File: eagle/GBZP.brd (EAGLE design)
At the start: 70 x 57.5 mm, 45 parts, among them CN1 USB-SMD-NS, J3 battery, X3 16MHz

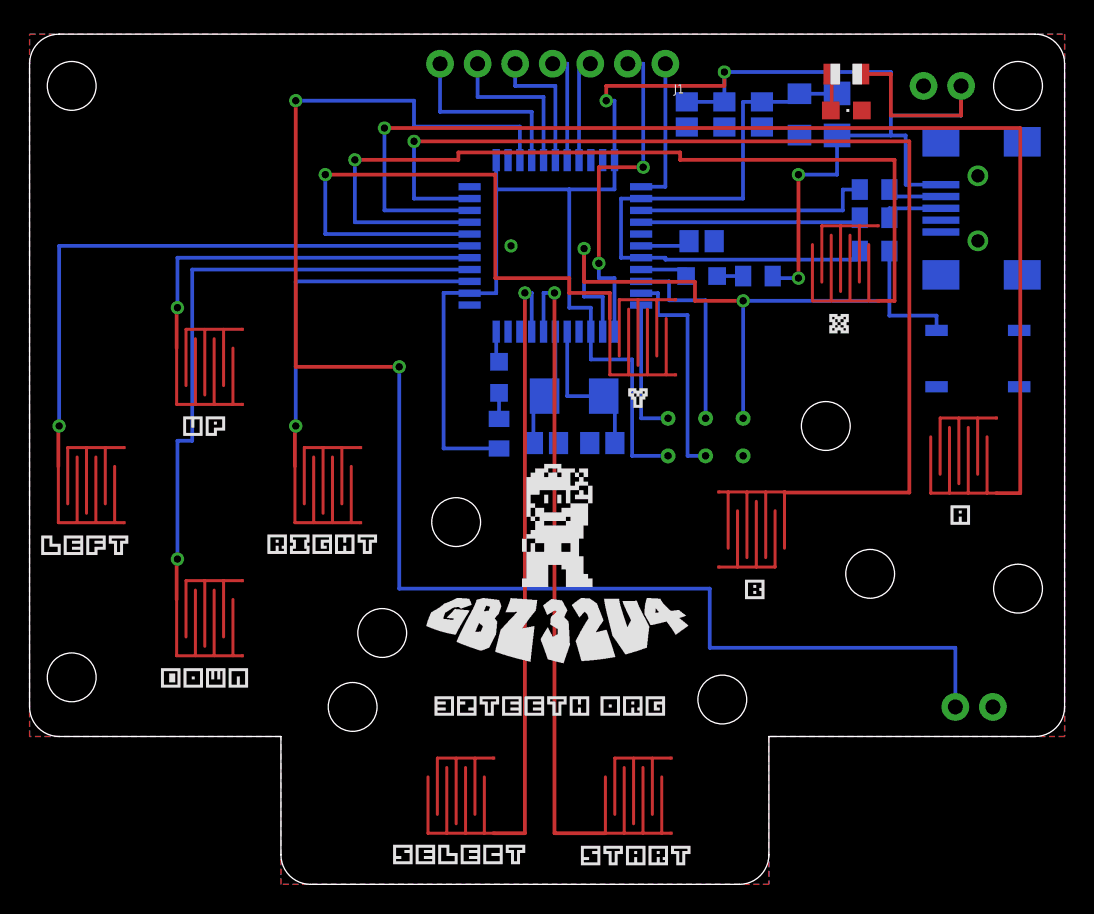
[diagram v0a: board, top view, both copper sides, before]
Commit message: new pinout to match GBZ project
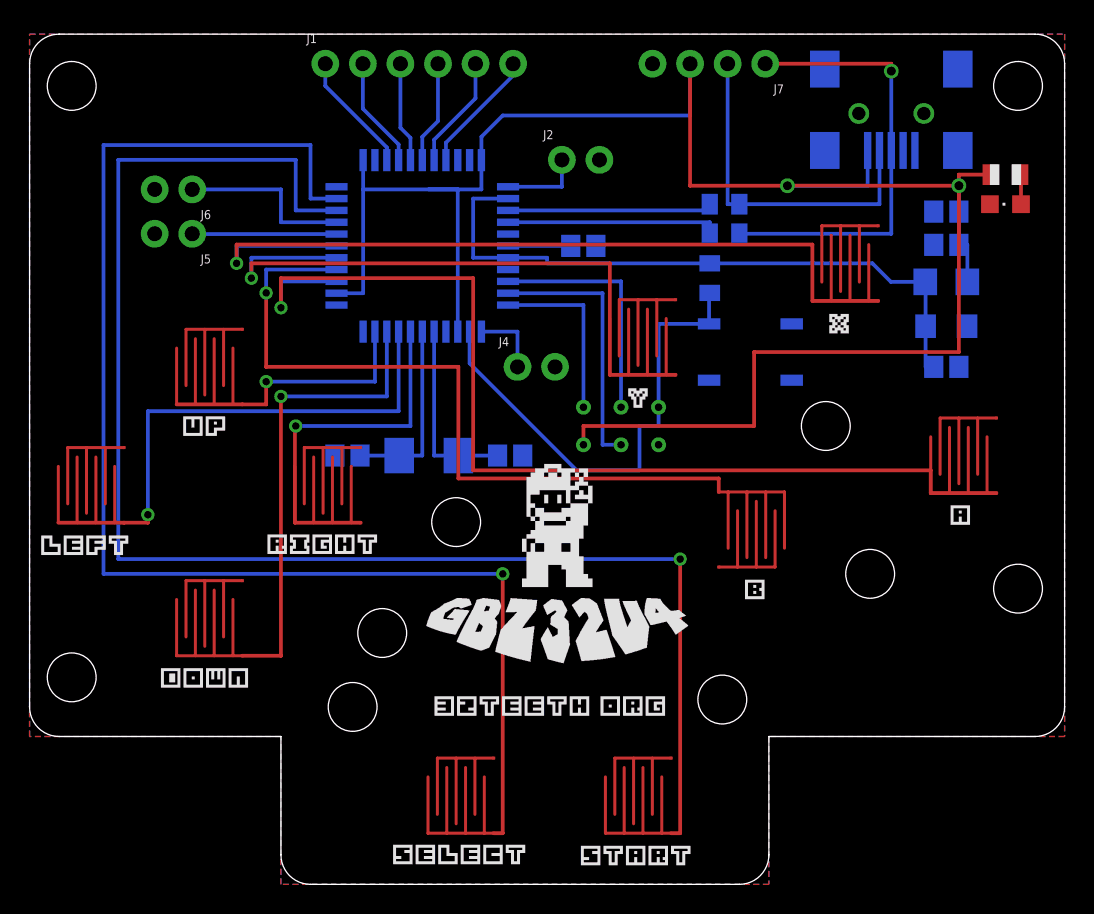
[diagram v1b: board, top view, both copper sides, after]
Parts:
- removed J3: battery, SparkFun-Connectors:1X02_NO_SILK
- removed JP2: Speaker, SparkFun-Connectors:1X02_NO_SILK
- removed LEDRX, LEDTX: LED, adafruit:CHIPLED_0805
- removed R4, R5: 100ohm, adafruit:R0805
- added J2, J4, J5, J6: (no value), SparkFun-Connectors:1X02_NO_SILK
- added J7: (no value), SparkFun-Connectors:1X04_NO_SILK
- J1: device SparkFun-Connectors:1X07_NO_SILK -> SparkFun-Connectors:1X06_NO_SILK
- moved J1 23.0 mm to (20.0, 55.5), turned to 0 degrees
- moved C4 21.1 mm to (62.0, 35.0), turned to 180 degrees
- moved C7 18.7 mm to (62.0, 45.5), turned to 0 degrees
- moved C5 17.4 mm to (62.0, 37.8), turned to 0 degrees
- moved C6 17.4 mm to (62.0, 43.2), turned to 0 degrees
- moved S1 15.4 mm to (48.8, 36.0)
- moved L1 13.5 mm to (62.0, 40.8), turned to 0 degrees
- moved C2 13.5 mm to (21.5, 29.0), turned to 0 degrees
- moved R2 12.7 mm to (66.0, 48.0), turned to 180 degrees
- moved LEDPWR 12.5 mm to (66.0, 46.0), turned to 90 degrees
- moved R6 11.3 mm to (46.0, 41.0), turned to 270 degrees
- moved X3 10.6 mm to (27.0, 29.0)
- moved R3 10.2 mm to (47.0, 44.0)
- moved R1 10.2 mm to (47.0, 46.0)
- moved U$2 9.00 mm to (26.6, 43.2)
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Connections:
- removed net A0/SPEAKER: JP2.2, U$2.36
- removed net D0/RX: U$2.20
- removed net D1/TX: U$2.21
- removed net D10/X: BTN-X.2, U$2.30
- removed net D11: J1.2, U$2.12
- removed net D12/DOWN: DIR-D.2, U$2.26
- removed net D13/B: BTN-B.2, U$2.32
- removed net D2/SELECT: BTN-SELECT.2, U$2.19
- removed net D3/START: BTN-START.2, U$2.18
- removed net D4/RIGHT: DIR-R.2, U$2.25
- removed net D5/A: BTN-A.2, U$2.31
- removed net D6/UP: DIR-U.2, U$2.27
- removed net D7: J1.1, U$2.1
- removed net D8/LEFT: DIR-L.2, U$2.28
- removed net D9/Y: BTN-Y.2, U$2.29
- removed net N$3: CN1.D+, R3.1
- removed net N$5: CN1.D-, R1.1
- removed net N$6: LEDRX.A, R4.1
- removed net N$7: LEDTX.A, R5.1
- new net A0: J1.1, U$2.36
- new net BTN_A: BTN-A.2, U$2.25
- new net BTN_B: BTN-B.2, U$2.26
- new net BTN_DOWN: DIR-D.2, U$2.20
- new net BTN_L1: J2.1, U$2.1
- new net BTN_L2: J4.1, U$2.12
- new net BTN_LEFT: DIR-L.2, U$2.19
- new net BTN_R1: J5.1, U$2.29
- new net BTN_R2: J6.1, U$2.30
- new net BTN_RIGHT: DIR-R.2, U$2.18
- new net BTN_SELECT: BTN-SELECT.2, U$2.32
- new net BTN_START: BTN-START.2, U$2.31
- new net BTN_UP: DIR-U.2, U$2.21
- new net BTN_X: BTN-X.2, U$2.28
- new net BTN_Y: BTN-Y.2, U$2.27
- new net D+IN: CN1.D+, J7.1, R3.1
- new net D-IN: CN1.D-, J7.2, R1.1
- net A1: now also J1.2; no longer J1.7
- net A2: now also J1.3; no longer J1.6
- net A3: now also J1.4; no longer J1.5
- net A4: now also J1.5; no longer J1.4
- net A5: now also J1.6; no longer J1.3
- net GND: now also J2.2, J4.2, J5.2, J6.2, J7.4; no longer J3.2, JP2.1
- net RXLED: no longer LEDRX.C
- net TXLED: no longer LEDTX.C
- net VCC: now also J7.3; no longer J3.1, R4.2, R5.2
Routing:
- net A0/SPEAKER: track 104.8 -> 0.00 mm, vias 2 -> 0
- net BTN_START: track 0.00 -> 102.3 mm, vias 0 -> 1
- net BTN_SELECT: track 0.00 -> 93.5 mm, vias 0 -> 1
- net D5/A: track 80.6 -> 0.00 mm, vias 1 -> 0
- net D13/B: track 73.4 -> 0.00 mm, vias 1 -> 0
- net BTN_A: track 0.00 -> 70.5 mm, vias 0 -> 1
- net D10/X: track 60.1 -> 0.00 mm, vias 1 -> 0
- net BTN_X: track 0.00 -> 56.4 mm, vias 0 -> 1
- net BTN_B: track 0.00 -> 50.4 mm, vias 0 -> 1
- net BTN_Y: track 0.00 -> 44.4 mm, vias 0 -> 1
- net D3/START: track 43.3 -> 0.00 mm, vias 1 -> 0
- net D9/Y: track 42.8 -> 0.00 mm, vias 1 -> 0
- net D8/LEFT: track 42.7 -> 0.00 mm, vias 1 -> 0
- net D12/DOWN: track 42.1 -> 0.00 mm, vias 1 -> 0
- net D2/SELECT: track 41.7 -> 0.00 mm, vias 1 -> 0
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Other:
- board text added: "(WH) D+ (GR) D- (RD) VCC (BK) GND"
- board text added: "A5 A4 A3 A2 A1 A0"
- board text removed: "D7 D11 A5 A4 A3 A2 A1"

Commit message: Mon Apr  3 10:04:51 EDT 2017 - added new pin mapping
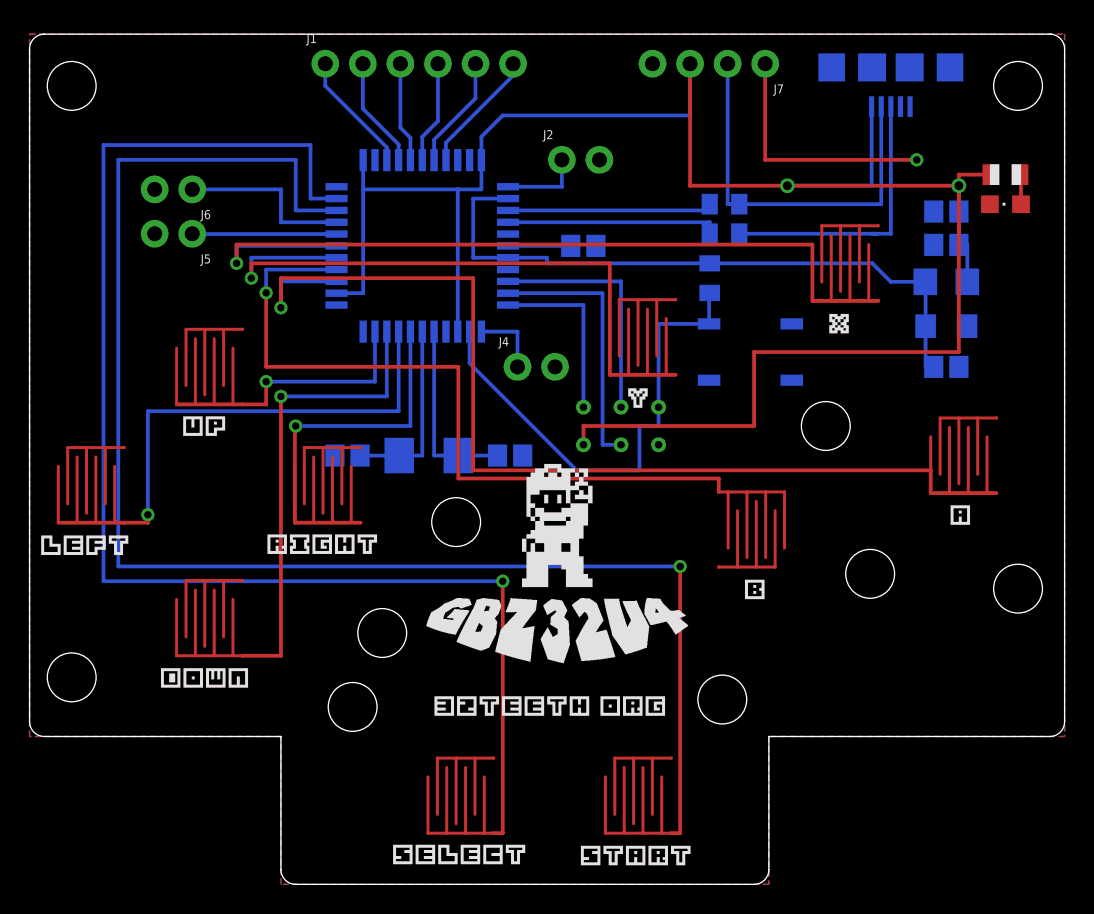
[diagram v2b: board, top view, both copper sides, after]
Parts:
- CN1: value USB-SMD-NS -> USB-MICROB; device SparkFun-Connectors:USB-MINIB-NOSTOP -> SparkFun-Connectors:USB-MICROB
- moved CN1 3.12 mm to (58.2, 55.2), turned to 180 degrees
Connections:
- net GND: now also CN1.MT1, CN1.MT2
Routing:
- net D+IN: track 30.3 -> 37.6 mm
- net D-IN: track 23.4 -> 26.5 mm
- net VCC: track 139.3 -> 140.5 mm
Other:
- outline, holes or cut-outs redrawn
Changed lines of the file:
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@@
 <board>
 <plain>
-<wire x1="70" y1="55.5" x2="70" y2="12" width="0" layer="20"/>
-<wire x1="70" y1="12" x2="68" y2="10" width="0" layer="20" curve="-90"/>
-<wire x1="68" y1="10" x2="50" y2="10" width="0" layer="20"/>
-<wire x1="70" y1="55.5" x2="68" y2="57.5" width="0" layer="20" curve="90"/>
-<wire x1="68" y1="57.5" x2="2" y2="57.5" width="0" layer="20"/>
-<wire x1="2" y1="57.5" x2="0" y2="55.5" width="0" layer="20" curve="90"/>
-<wire x1="0" y1="55.5" x2="0" y2="12" width="0" layer="20"/>
-<wire x1="0" y1="12" x2="2" y2="10" width="0" layer="20" curve="90"/>
-<wire x1="2" y1="10" x2="17" y2="10" width="0" layer="20"/>
-<wire x1="50" y1="10" x2="50" y2="2" width="0" layer="20"/>
-<wire x1="50" y1="2" x2="48" y2="0" width="0" layer="20" curve="-90"/>
-<wire x1="48" y1="0" x2="19" y2="0" width="0" layer="20"/>
-<wire x1="19" y1="0" x2="17" y2="2" width="0" layer="20" curve="-90"/>
-<wire x1="17" y1="2" x2="17" y2="10" width="0" layer="20"/>
+<wire x1="70" y1="11" x2="70" y2="56.5" width="0" layer="20"/>
+<wire x1="70" y1="56.5" x2="69" y2="57.5" width="0" layer="20" curve="90"/>
+<wire x1="69" y1="57.5" x2="1" y2="57.5" width="0" layer="20"/>
+<wire x1="70" y1="11" x2="69" y2="10" width="0" layer="20" curve="-90"/>
+<wire x1="69" y1="10" x2="50" y2="10" width="0" layer="20"/>
+<wire x1="1" y1="57.5" x2="0" y2="56.5" width="0" layer="20" curve="90"/>
+<wire x1="0" y1="56.5" x2="0" y2="11" width="0" layer="20"/>
+<wire x1="0" y1="11" x2="1" y2="10" width="0" layer="20" curve="90"/>
+<wire x1="1" y1="10" x2="17" y2="10" width="0" layer="20"/>
+<wire x1="50" y1="10" x2="50" y2="1" width="0" layer="20"/>
+<wire x1="50" y1="1" x2="49" y2="0" width="0" layer="20" curve="-90"/>
+<wire x1="49" y1="0" x2="18" y2="0" width="0" layer="20"/>
+<wire x1="18" y1="0" x2="17" y2="1" width="0" layer="20" curve="-90"/>
+<wire x1="17" y1="1" x2="17" y2="10" width="0" layer="20"/>
 <rectangle x1="27.3846" y1="11.4002" x2="28.7054" y2="11.451" layer="21"/>
 <rectangle x1="28.9086" y1="11.4002" x2="30.2294" y2="11.451" layer="21"/>
@@
 <element name="C6" library="adafruit" package="C0805" value="0.1uF" x="62" y="43.25" smashed="yes" rot="MR0"/>
 <element name="C7" library="adafruit" package="C0805" value="0.1uF" x="62" y="45.5" smashed="yes" rot="MR0"/>
-<element name="CN1" library="SparkFun-Connectors" package="USB-MINIB-NOSTOP" value="USB-SMD-NS" x="58.28" y="52.135" smashed="yes" rot="MR270"/>
+<element name="CN1" library="SparkFun-Connectors" package="USB-MICROB" value="USB-MICROB" x="58.25" y="55.25" smashed="yes" rot="MR180">
+<attribute name="PROD_ID" value="CONN-09505" x="58.25" y="55.25" size="1.778" layer="28" rot="MR180" display="off"/>
+</element>
 <element name="R2" library="adafruit" package="R0805" value="100ohm" x="66" y="48" smashed="yes" rot="R180"/>
 <element name="LEDPWR" library="adafruit" package="CHIPLED_0805" value="LED" x="66" y="46" smashed="yes" rot="R90"/>
@@
 <contactref element="J6" pad="2"/>
 <contactref element="J7" pad="4"/>
+<contactref element="CN1" pad="MT1"/>
+<contactref element="CN1" pad="MT2"/>
 <wire x1="38.3" y1="43.18" x2="39.88" y2="39.54" width="0" layer="19" extent="1-16"/>
 <wire x1="32.36" y1="43.98" x2="29.76" y2="48.98" width="0" layer="19" extent="16-16"/>
@@
 <wire x1="44.67" y1="47.25" x2="51.25" y2="47.25" width="0.254" layer="1"/>
 <wire x1="62.85" y1="47.25" x2="51.25" y2="47.25" width="0.254" layer="1"/>
-<wire x1="56.68" y1="49.635" x2="56.68" y2="47.25" width="0.254" layer="16"/>
-<wire x1="56.68" y1="47.25" x2="51.25" y2="47.25" width="0.254" layer="16"/>
 <via x="51.25" y="47.25" extent="1-16" drill="0.6"/>
 <wire x1="62.85" y1="47.25" x2="62.85" y2="45.5" width="0.254" layer="16"/>
@@
 <wire x1="30.56" y1="47" x2="30.56" y2="48.98" width="0.254" layer="16"/>
 <wire x1="22.56" y1="48.98" x2="22.56" y2="47" width="0.254" layer="16"/>
-<wire x1="27" y1="47" x2="30.56" y2="47" width="0.254" layer="16"/>
-<wire x1="27" y1="47" x2="22.56" y2="47" width="0.254" layer="16"/>
+<wire x1="28.96" y1="47" x2="30.56" y2="47" width="0.254" layer="16"/>
+<wire x1="28.96" y1="47" x2="22.56" y2="47" width="0.254" layer="16"/>
 <wire x1="22.56" y1="47" x2="22.56" y2="39.98" width="0.254" layer="16"/>
 <wire x1="22.56" y1="39.98" x2="20.76" y2="39.98" width="0.254" layer="16"/>
@@
 <wire x1="62.85" y1="36" x2="62.85" y2="47.25" width="0.254" layer="1"/>
 <wire x1="49" y1="36" x2="62.85" y2="36" width="0.254" layer="1"/>
-<wire x1="28.96" y1="47" x2="27" y2="47" width="0.254" layer="16"/>
 <wire x1="28.96" y1="37.38" x2="28.96" y2="47" width="0.254" layer="16"/>
+<wire x1="56.95" y1="52.6" x2="56.95" y2="47.25" width="0.254" layer="16"/>
+<wire x1="56.95" y1="47.25" x2="51.25" y2="47.25" width="0.254" layer="16"/>
 </signal>
 <signal name="BTN_UP">
@@
 <contactref element="R3" pad="1"/>
 <contactref element="J7" pad="1"/>
-<wire x1="49.75" y1="55.5" x2="58.28" y2="55.5" width="0.254" layer="1"/>
-<wire x1="58.28" y1="55.5" x2="58.28" y2="55" width="0.254" layer="1"/>
-<via x="58.28" y="55" extent="1-16" drill="0.6"/>
-<wire x1="58.28" y1="49.635" x2="58.28" y2="55" width="0.254" layer="16"/>
-<wire x1="48" y1="44" x2="58.28" y2="44" width="0.254" layer="16"/>
-<wire x1="58.28" y1="44" x2="58.28" y2="49.635" width="0.254" layer="16"/>
+<wire x1="57" y1="44" x2="48" y2="44" width="0.254" layer="16"/>
+<wire x1="57" y1="44" x2="57.28" y2="44" width="0.254" layer="16"/>
+<wire x1="58.25" y1="49" x2="58.25" y2="52.6" width="0.254" layer="16"/>
+<wire x1="58.25" y1="49" x2="58.25" y2="44" width="0.254" layer="16"/>
+<wire x1="58.25" y1="44" x2="57" y2="44" width="0.254" layer="16"/>
+<wire x1="49.75" y1="55.5" x2="49.75" y2="49" width="0.254" layer="1"/>
+<wire x1="49.75" y1="49" x2="60" y2="49" width="0.254" layer="1"/>
+<via x="60" y="49" extent="1-16" drill="0.5"/>
+<wire x1="60" y1="49" x2="58.25" y2="49" width="0.254" layer="16"/>
 </signal>
 <signal name="D-IN">
@@
 <contactref element="J7" pad="2"/>
 <wire x1="47.21" y1="55.5" x2="47.21" y2="46" width="0.254" layer="16"/>
-<wire x1="47.21" y1="46" x2="48" y2="46" width="0.254" layer="16"/>
-<wire x1="48" y1="46" x2="57.48" y2="46" width="0.254" layer="16"/>
-<wire x1="57.48" y1="46" x2="57.48" y2="49.635" width="0.254" layer="16"/>
+<wire x1="48" y1="46" x2="47.21" y2="46" width="0.254" layer="16"/>
+<wire x1="57.6" y1="52.6" x2="57.6" y2="46" width="0.254" layer="16"/>
+<wire x1="57.6" y1="46" x2="48" y2="46" width="0.254" layer="16"/>
 </signal>
 <signal name="D-">
@@
 <wire x1="18" y1="49" x2="6" y2="49" width="0.254" layer="16"/>
 <wire x1="18" y1="45.58" x2="18" y2="49" width="0.254" layer="16"/>
-<wire x1="6" y1="22" x2="44" y2="22" width="0.254" layer="16"/>
-<wire x1="6" y1="49" x2="6" y2="22" width="0.254" layer="16"/>
-<via x="44" y="22" extent="1-16" drill="0.5"/>
-<wire x1="44" y1="22" x2="44" y2="3.46" width="0.254" layer="1"/>
+<wire x1="6" y1="21.5" x2="44" y2="21.5" width="0.254" layer="16"/>
+<wire x1="6" y1="49" x2="6" y2="21.5" width="0.254" layer="16"/>
+<via x="44" y="21.5" extent="1-16" drill="0.5"/>
+<wire x1="44" y1="21.5" x2="44" y2="3.46" width="0.254" layer="1"/>
 <wire x1="44" y1="3.46" x2="43.39" y2="3.46" width="0.254" layer="1"/>
 </signal>
@@
 <wire x1="19" y1="46.38" x2="19" y2="50" width="0.254" layer="16"/>
 <wire x1="19" y1="50" x2="5" y2="50" width="0.254" layer="16"/>
-<wire x1="5" y1="50" x2="5" y2="21" width="0.254" layer="16"/>
-<via x="32" y="21" extent="1-16" drill="0.5"/>
-<wire x1="32" y1="21" x2="32" y2="3.46" width="0.254" layer="1"/>
+<wire x1="5" y1="50" x2="5" y2="20.5" width="0.254" layer="16"/>
+<via x="32" y="20.5" extent="1-16" drill="0.5"/>
+<wire x1="32" y1="20.5" x2="32" y2="3.46" width="0.254" layer="1"/>
 <wire x1="32" y1="3.46" x2="31.39" y2="3.46" width="0.254" layer="1"/>
-<wire x1="5" y1="21" x2="32" y2="21" width="0.254" layer="16"/>
+<wire x1="5" y1="20.5" x2="32" y2="20.5" width="0.254" layer="16"/>
 </signal>
 <signal name="BTN_L1">
